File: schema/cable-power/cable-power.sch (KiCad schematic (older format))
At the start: 2 parts, among them P1 CONN_6, P2 CONN_6

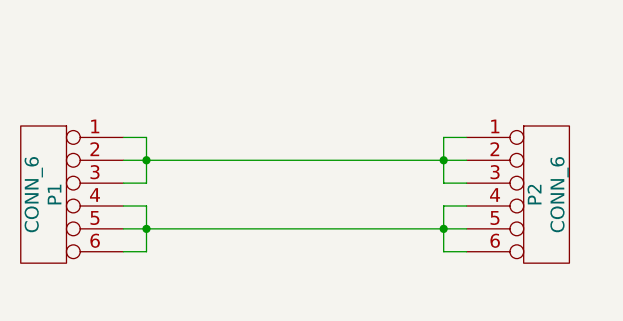
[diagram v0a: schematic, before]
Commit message: Vavle and power cables for new schemas.
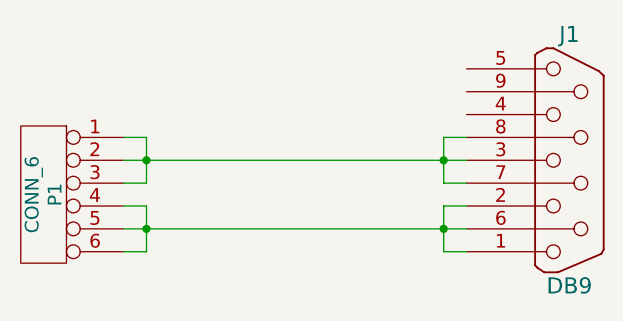
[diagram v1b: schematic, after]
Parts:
- removed P2: CONN_6, symbol CONN_6
- added J1: DB9, symbol DB9
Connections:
- net at P1.1, P1.2, P1.3: now also J1.3, J1.7 (P7), J1.8 (P8)
- net at P1.4, P1.5, P1.6: now also J1.1, J1.2, J1.6 (P6)
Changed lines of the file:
@@
-EESchema Schematic File Version 2  date Wed 05 Sep 2012 02:15:02 PM MSK
+EESchema Schematic File Version 2  date Wed 03 Oct 2012 09:32:51 PM MSK
 LIBS:power
 LIBS:device
@@
 Sheet 1 1
 Title ""
-Date "5 sep 2012"
+Date "3 oct 2012"
 Rev ""
 Comp ""
@@
 Comment4 ""
 $EndDescr
+$Comp
+L DB9 J1
+U 1 1 506C76A3
+P 6750 3800
+F 0 "J1" H 6750 4350 70  0000 C CNN
+F 1 "DB9" H 6750 3250 70  0000 C CNN
+	1    6750 3800
+	1    0    0    -1
+$EndComp
 Wire Wire Line
 	4800 4100 6300 4100
@@
 	-1   0    0    -1
 $EndComp
-$Comp
-L CONN_6 P2
-U 1 1 503B6DBE
-P 6650 3950
-F 0 "P2" V 6600 3950 60  0000 C CNN
-F 1 "CONN_6" V 6700 3950 60  0000 C CNN
-	1    6650 3950
-	1    0    0    -1
-$EndComp
 $EndSCHEMATC
